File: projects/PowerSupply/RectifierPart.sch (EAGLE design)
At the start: 12 parts, among them X1 IN, X2 PRI, X3 SEC, X4 OUT

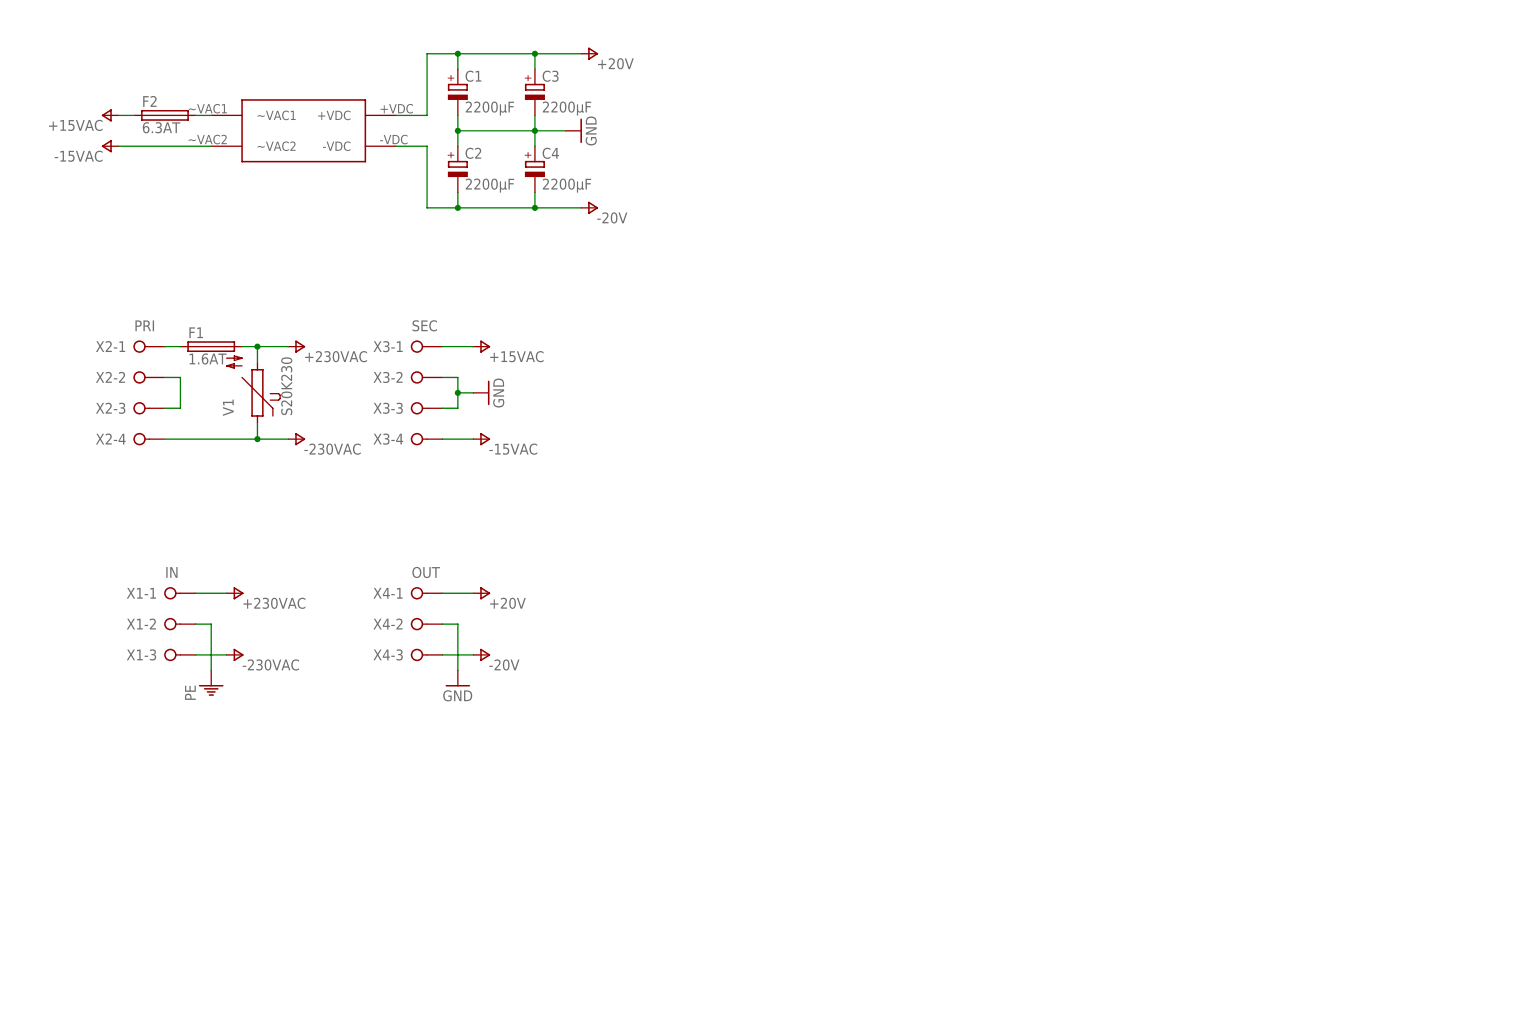
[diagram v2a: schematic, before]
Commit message: feat: rectifier part modified
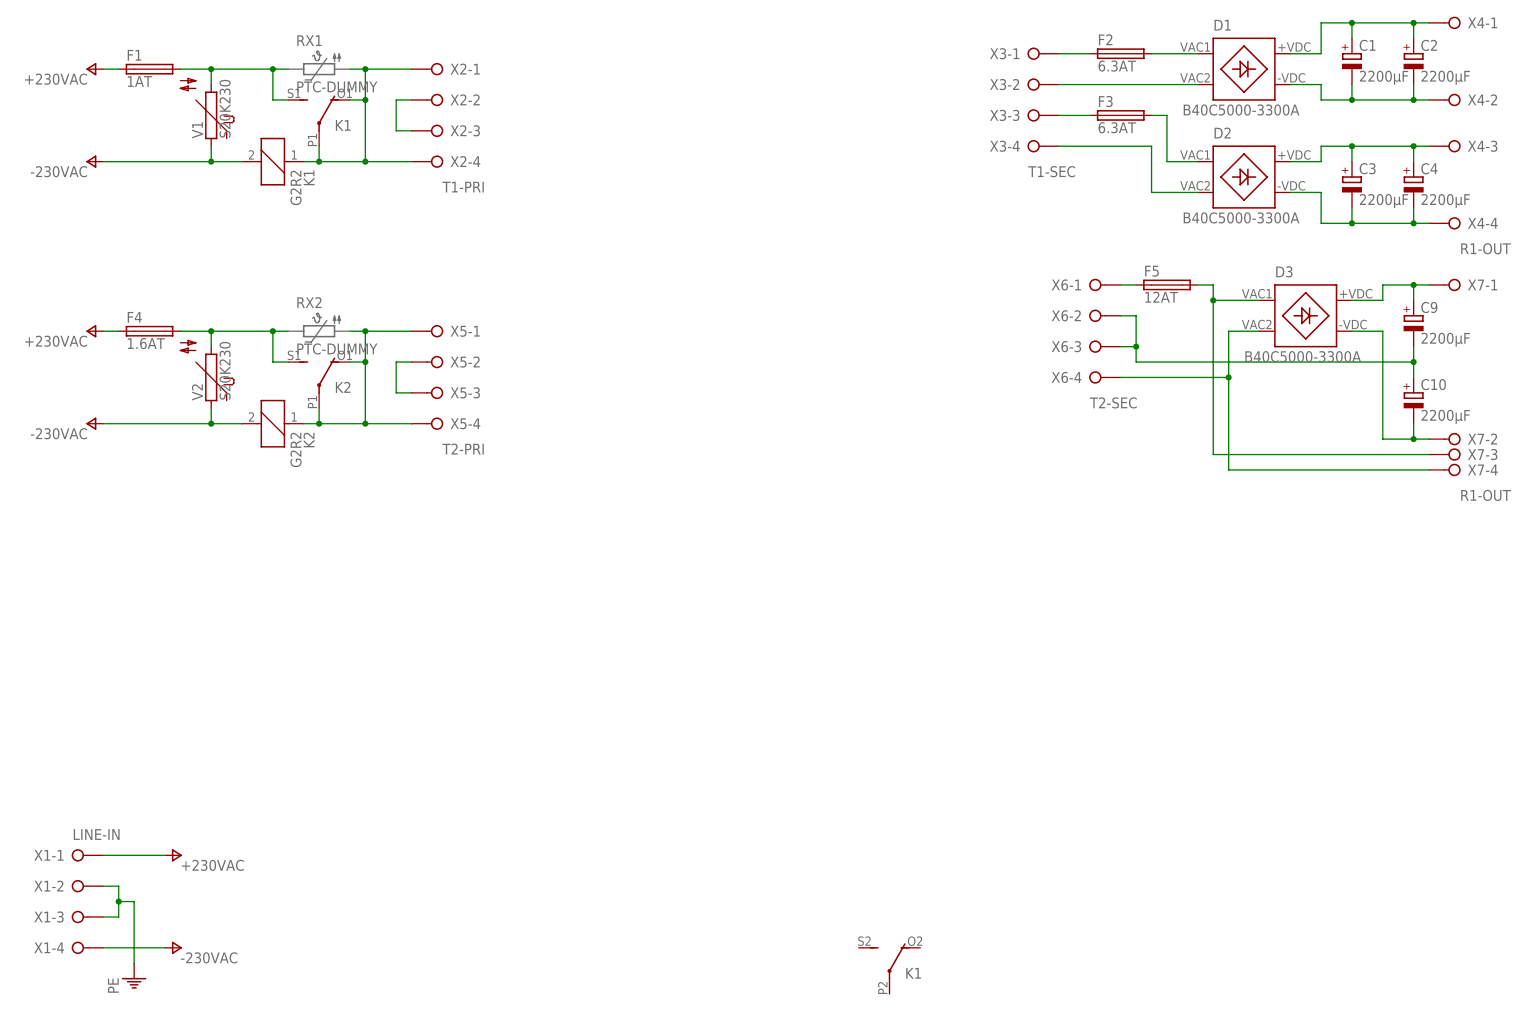
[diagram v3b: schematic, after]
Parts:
- removed R+1: B40C5000-3300A, bb84:B40C5000-3300A
- added C10, C9: 2200µF, rcl:CPOL-EUE7.5-16
- added D1, D2, D3: B40C5000-3300A, bb84:B40C5000-3300A
- added F3: 6.3AT, fuse:SH22,5A
- added F4: 1.6AT, fuse:SH22,5A
- added F5: 12AT, fuse:SH22,5A
- added K1, K2: G2R2, relay:G2R2
- added V2: S20K230, varistor:S20K230
- added X5: T2-PRI, con-wago-508:W237-04P
- added X6: T2-SEC, con-wago-508:W237-04P
- added X7: R1-OUT, con-wago-508:W237-04P
- F1: value 1.6AT -> 1AT
- X1: value IN -> LINE-IN; device con-wago-508:W237-03P -> con-wago-508:W237-04P
- X2: value PRI -> T1-PRI
- X3: value SEC -> T1-SEC
- X4: value OUT -> R1-OUT; device con-wago-508:W237-03P -> con-wago-508:W237-04P
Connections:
- net +15VAC renamed N$8
- removed net +20V: C1.+, C3.+, R+1.+VDC, X4-1.KL
- removed net -15VAC: R+1.~VAC2, X3-4.KL
- removed net -20V: C2.-, C4.-, R+1.-VDC, X4-3.KL
- removed net GND: C1.-, C2.+, C3.-, C4.+, X3-2.KL, X3-3.KL, X4-2.KL
- new net N$10: D1.VAC1, F2.2
- new net N$11: F4.2, K22.S, V2.2
- new net N$12: K21.1, K22.O, K22.P, X5-1.KL, X5-4.KL
- new net N$13: F3.1, X3-3.KL
- new net N$14: D2.VAC1, F3.2
- new net N$15: D2.VAC2, X3-4.KL
- new net N$16: X5-2.KL, X5-3.KL
- new net N$17: F5.1, X6-1.KL
- new net N$18: D3.VAC1, F5.2, X7-3.KL
- new net N$19: D3.VAC2, X6-4.KL, X7-4.KL
- new net N$2: K11.1, K12.O, K12.P, X2-1.KL, X2-4.KL
- new net N$20: C9.+, D3.+VDC, X7-1.KL
- new net N$21: C10.-, D3.-VDC, X7-2.KL
- new net N$22: C10.+, C9.-, X6-2.KL, X6-3.KL
- new net N$4: C1.+, C2.+, D1.+VDC, X4-1.KL
- new net N$6: C3.+, C4.+, D2.+VDC, X4-3.KL
- new net N$7: C1.-, C2.-, D1.-VDC, X4-2.KL
- new net N$9: C3.-, C4.-, D2.-VDC, X4-4.KL
- net +230VAC: now also F1.1, F4.1; no longer F1.2, V1.2
- net -230VAC: now also K11.2, K21.2, V2.1, X1-4.KL; no longer X1-3.KL, X2-4.KL
- net N$1: now also D1.VAC2, X3-2.KL; no longer F2.2, R+1.~VAC1
- net N$3: now also F1.2, K12.S, V1.2; no longer F1.1, X2-1.KL
- net PE: now also X1-3.KL
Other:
- moved on the sheet: C1, C2, C3, C4, F1, F2, V1, X1-1, X1-2, X1-3, X2-1, X2-2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

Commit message: feat: rectifier part modified
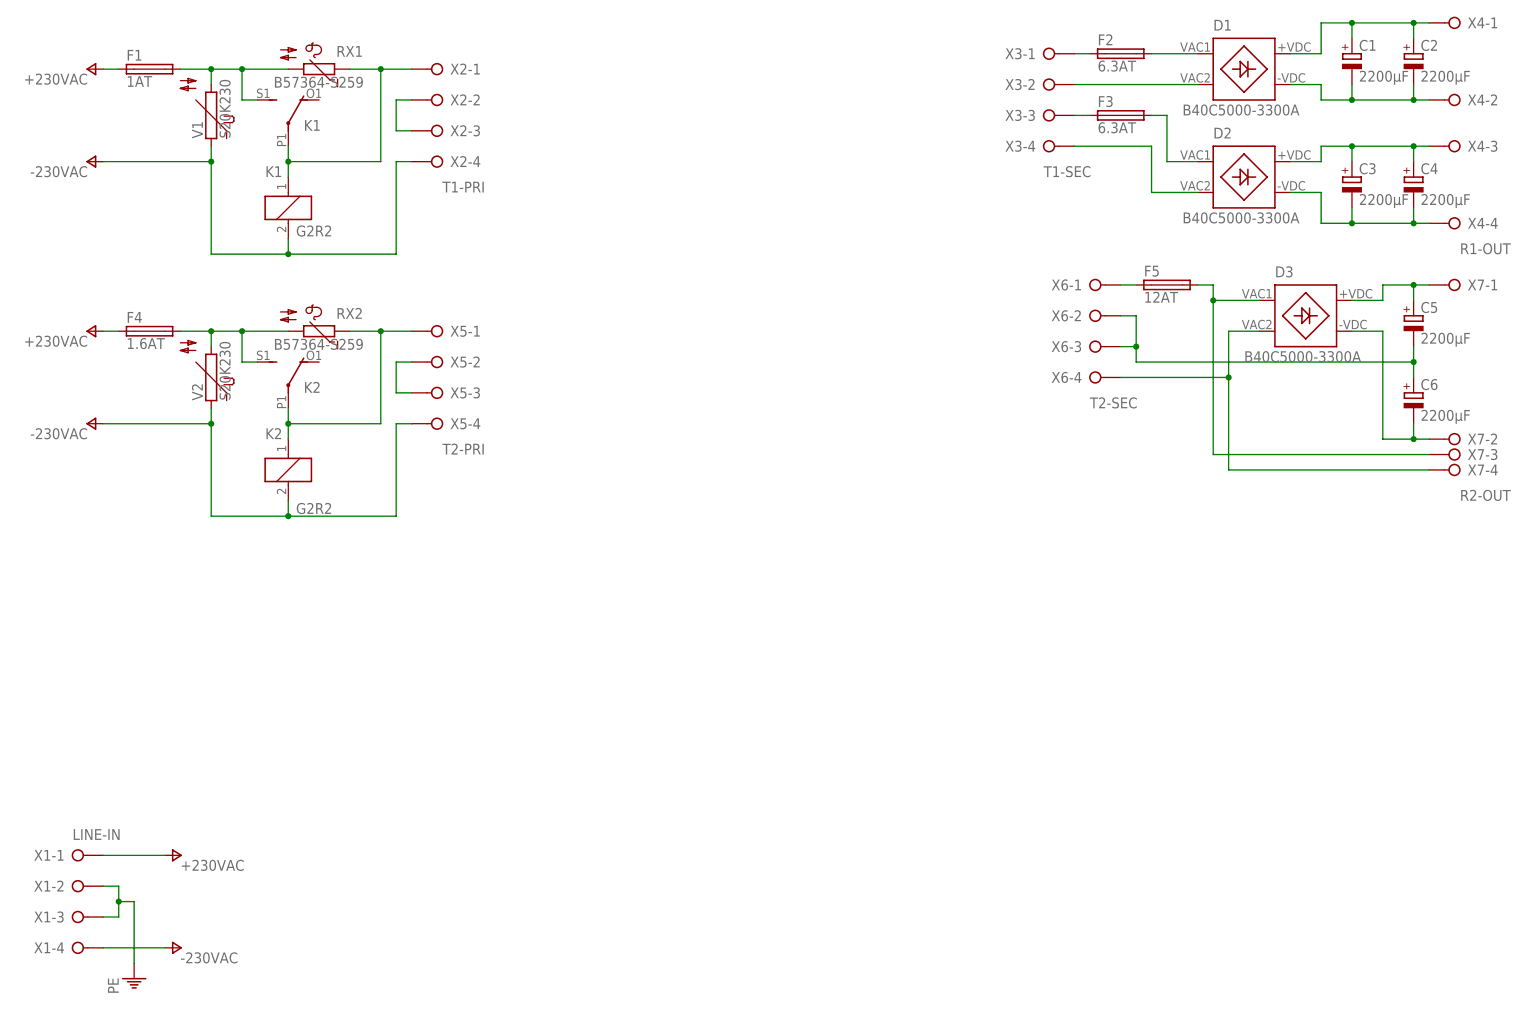
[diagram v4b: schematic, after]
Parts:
- added RX1, RX2: B57364-S259, bb84:EPCB57364-S259
- X7: value R1-OUT -> R2-OUT
- renumbered C10 to C6, C9 to C5
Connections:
- removed net N$12: K21.1, K22.O, K22.P, X5-1.KL, X5-4.KL
- new net N$24: K21.1, K22.P, RX2.1, X5-1.KL
- net -230VAC: now also X2-4.KL, X5-4.KL
- net N$11: now also RX2.2
- net N$2: now also RX1.1; no longer K12.O, X2-4.KL
- net N$3: now also RX1.2
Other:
- moved on the sheet: K1, K2, X3-1, X3-2, X3-3, X3-4

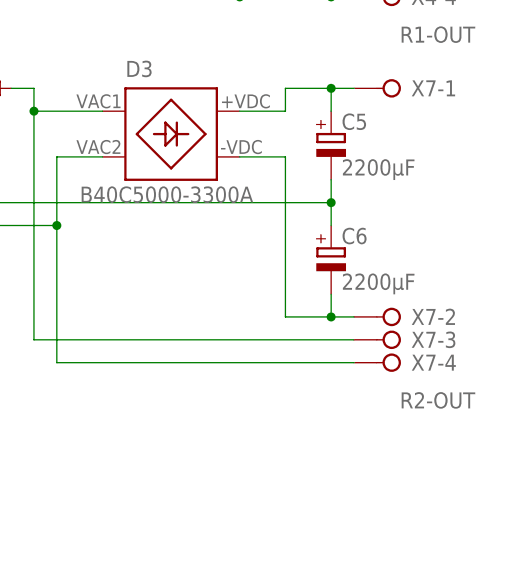
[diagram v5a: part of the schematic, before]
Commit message: feat: rectifier changes applied
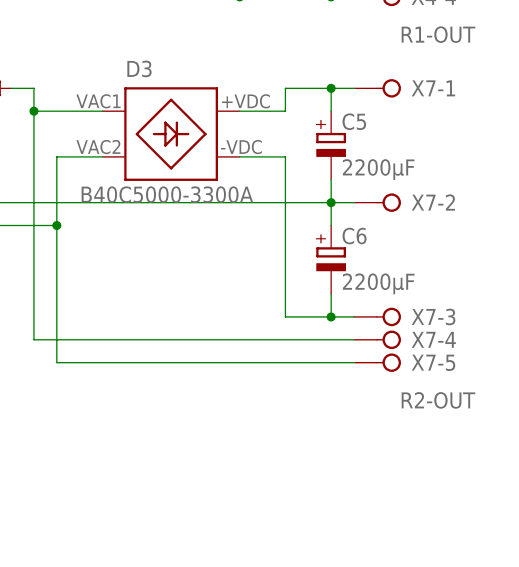
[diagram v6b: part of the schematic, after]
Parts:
- X7: device con-wago-508:W237-04P -> con-wago-508:W237-05P
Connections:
- net N$18: now also X7-4.KL; no longer X7-3.KL
- net N$19: now also X7-5.KL; no longer X7-4.KL
- net N$21: now also X7-3.KL; no longer X7-2.KL
- net N$22: now also X7-2.KL
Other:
- moved on the sheet: X7-2, X7-3, X7-4
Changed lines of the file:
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@@
 <part name="X6" library="con-wago-508" library_urn="urn:adsk.eagle:library:196" deviceset="W237-04P" device="" package3d_urn="urn:adsk.eagle:package:10735/1" value="T2-SEC"/>
 <part name="F5" library="fuse" library_urn="urn:adsk.eagle:library:233" deviceset="SH22,5A" device="" package3d_urn="urn:adsk.eagle:package:14070/1" value="12AT"/>
-<part name="X7" library="con-wago-508" library_urn="urn:adsk.eagle:library:196" deviceset="W237-04P" device="" package3d_urn="urn:adsk.eagle:package:10735/1" value="R2-OUT"/>
 <part name="D3" library="bb84" deviceset="B40C5000-3300A" device="" value="B40C5000-3300A"/>
 <part name="C5" library="rcl" library_urn="urn:adsk.eagle:library:334" deviceset="CPOL-EU" device="E7.5-16" package3d_urn="urn:adsk.eagle:package:23382/2" value="2200µF"/>
@@
 <part name="RX1" library="bb84" deviceset="EPCB57364-S259" device="" value="B57364-S259"/>
 <part name="RX2" library="bb84" deviceset="EPCB57364-S259" device="" value="B57364-S259"/>
+<part name="X7" library="con-wago-508" library_urn="urn:adsk.eagle:library:196" deviceset="W237-05P" device="" package3d_urn="urn:adsk.eagle:package:10736/1" value="R2-OUT"/>
 </parts>
 <sheets>
@@
 <attribute name="VALUE" x="191.77" y="124.079" size="1.778" layer="96"/>
 </instance>
-<instance part="X7" gate="-1" x="243.84" y="127" smashed="yes" rot="MR0">
-<attribute name="NAME" x="245.11" y="127.889" size="1.778" layer="95" rot="MR180"/>
-</instance>
-<instance part="X7" gate="-2" x="243.84" y="101.6" smashed="yes" rot="MR0">
-<attribute name="NAME" x="245.11" y="102.489" size="1.778" layer="95" rot="MR180"/>
-</instance>
-<instance part="X7" gate="-3" x="243.84" y="99.06" smashed="yes" rot="MR0">
-<attribute name="NAME" x="245.11" y="99.949" size="1.778" layer="95" rot="MR180"/>
-</instance>
-<instance part="X7" gate="-4" x="243.84" y="96.52" smashed="yes" rot="MR0">
-<attribute name="VALUE" x="243.84" y="91.44" size="1.778" layer="96"/>
-<attribute name="NAME" x="245.11" y="97.409" size="1.778" layer="95" rot="MR180"/>
-</instance>
 <instance part="D3" gate="G$1" x="218.44" y="121.92" smashed="yes">
 <attribute name="NAME" x="213.36" y="128.27" size="1.778" layer="95"/>
@@
 <attribute name="NAME" x="58.6994" y="121.412" size="1.778" layer="95"/>
 <attribute name="VALUE" x="48.387" y="116.332" size="1.778" layer="96"/>
+</instance>
+<instance part="X7" gate="-1" x="243.84" y="127" smashed="yes" rot="MR0">
+<attribute name="NAME" x="245.11" y="127.889" size="1.778" layer="95" rot="MR180"/>
+</instance>
+<instance part="X7" gate="-2" x="243.84" y="114.3" smashed="yes" rot="MR0">
+<attribute name="NAME" x="245.11" y="115.189" size="1.778" layer="95" rot="MR180"/>
+</instance>
+<instance part="X7" gate="-3" x="243.84" y="101.6" smashed="yes" rot="MR0">
+<attribute name="NAME" x="245.11" y="102.489" size="1.778" layer="95" rot="MR180"/>
+</instance>
+<instance part="X7" gate="-4" x="243.84" y="99.06" smashed="yes" rot="MR0">
+<attribute name="NAME" x="245.11" y="99.949" size="1.778" layer="95" rot="MR180"/>
+</instance>
+<instance part="X7" gate="-5" x="243.84" y="96.52" smashed="yes" rot="MR0">
+<attribute name="VALUE" x="243.84" y="91.44" size="1.778" layer="96"/>
+<attribute name="NAME" x="245.11" y="97.409" size="1.778" layer="95" rot="MR180"/>
 </instance>
 </instances>
@@
 <pinref part="F5" gate="1" pin="2"/>
 <wire x1="203.2" y1="127" x2="200.66" y2="127" width="0.1524" layer="91"/>
-<pinref part="X7" gate="-3" pin="KL"/>
 <wire x1="203.2" y1="124.46" x2="203.2" y2="99.06" width="0.1524" layer="91"/>
 <wire x1="203.2" y1="99.06" x2="238.76" y2="99.06" width="0.1524" layer="91"/>
 <junction x="203.2" y="124.46"/>
+<pinref part="X7" gate="-4" pin="KL"/>
 </segment>
 </net>
 <net name="N$19" class="0">
 <segment>
-<pinref part="X7" gate="-4" pin="KL"/>
 <wire x1="205.74" y1="96.52" x2="238.76" y2="96.52" width="0.1524" layer="91"/>
 <pinref part="D3" gate="G$1" pin="VAC2"/>
@@
 <wire x1="205.74" y1="96.52" x2="205.74" y2="111.76" width="0.1524" layer="91"/>
 <junction x="205.74" y="111.76"/>
+<pinref part="X7" gate="-5" pin="KL"/>
 </segment>
 </net>
@@
 <wire x1="226.06" y1="124.46" x2="231.14" y2="124.46" width="0.1524" layer="91"/>
 <wire x1="231.14" y1="124.46" x2="231.14" y2="127" width="0.1524" layer="91"/>
-<pinref part="X7" gate="-1" pin="KL"/>
 <pinref part="C5" gate="G$1" pin="+"/>
 <wire x1="238.76" y1="127" x2="236.22" y2="127" width="0.1524" layer="91"/>
@@
 <wire x1="236.22" y1="127" x2="236.22" y2="124.46" width="0.1524" layer="91"/>
 <junction x="236.22" y="127"/>
+<pinref part="X7" gate="-1" pin="KL"/>
 </segment>
 </net>
@@
 <wire x1="226.06" y1="119.38" x2="231.14" y2="119.38" width="0.1524" layer="91"/>
 <wire x1="231.14" y1="119.38" x2="231.14" y2="101.6" width="0.1524" layer="91"/>
-<pinref part="X7" gate="-2" pin="KL"/>
 <pinref part="C6" gate="G$1" pin="-"/>
 <wire x1="238.76" y1="101.6" x2="236.22" y2="101.6" width="0.1524" layer="91"/>
@@
 <wire x1="236.22" y1="101.6" x2="236.22" y2="104.14" width="0.1524" layer="91"/>
 <junction x="236.22" y="101.6"/>
+<pinref part="X7" gate="-3" pin="KL"/>
 </segment>
 </net>
@@
 <wire x1="190.5" y1="116.84" x2="187.96" y2="116.84" width="0.1524" layer="91"/>
 <junction x="190.5" y="116.84"/>
-</segment>
-</net>
+<pinref part="X7" gate="-2" pin="KL"/>
+<wire x1="238.76" y1="114.3" x2="236.22" y2="114.3" width="0.1524" layer="91"/>
+</segment>
+</net>
